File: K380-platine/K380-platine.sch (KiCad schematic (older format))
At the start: 32 parts, among them J1 JST-PH 2, J2 Conn_01x23, J3 MicroMod-M.2E, J4 USB_C_Receptacle_USB2.0, J5 Conn_ARM_JTAG_SWD_10, Q1 PMost Enc FET -20V, Q2 Q_NMOS_DGS, SW1 EG1215AA, SW2 SW_Push, SW3 SW_Push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

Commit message: Finished basic layout
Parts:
- Q2: symbol Device:Q_NMOS_DGS -> Device:Q_NMOS_DSG
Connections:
- net VBAT: now also Q2.2 (S); no longer Q2.3 (S)
- net at R7.1: now also Q2.3 (G); no longer Q2.2 (G)
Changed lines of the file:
@@
 $EndComp
 $Comp
-L Device:Q_NMOS_DGS Q2
+L Device:Q_NMOS_DSG Q2
 U 1 1 62992380
 P 1750 9150

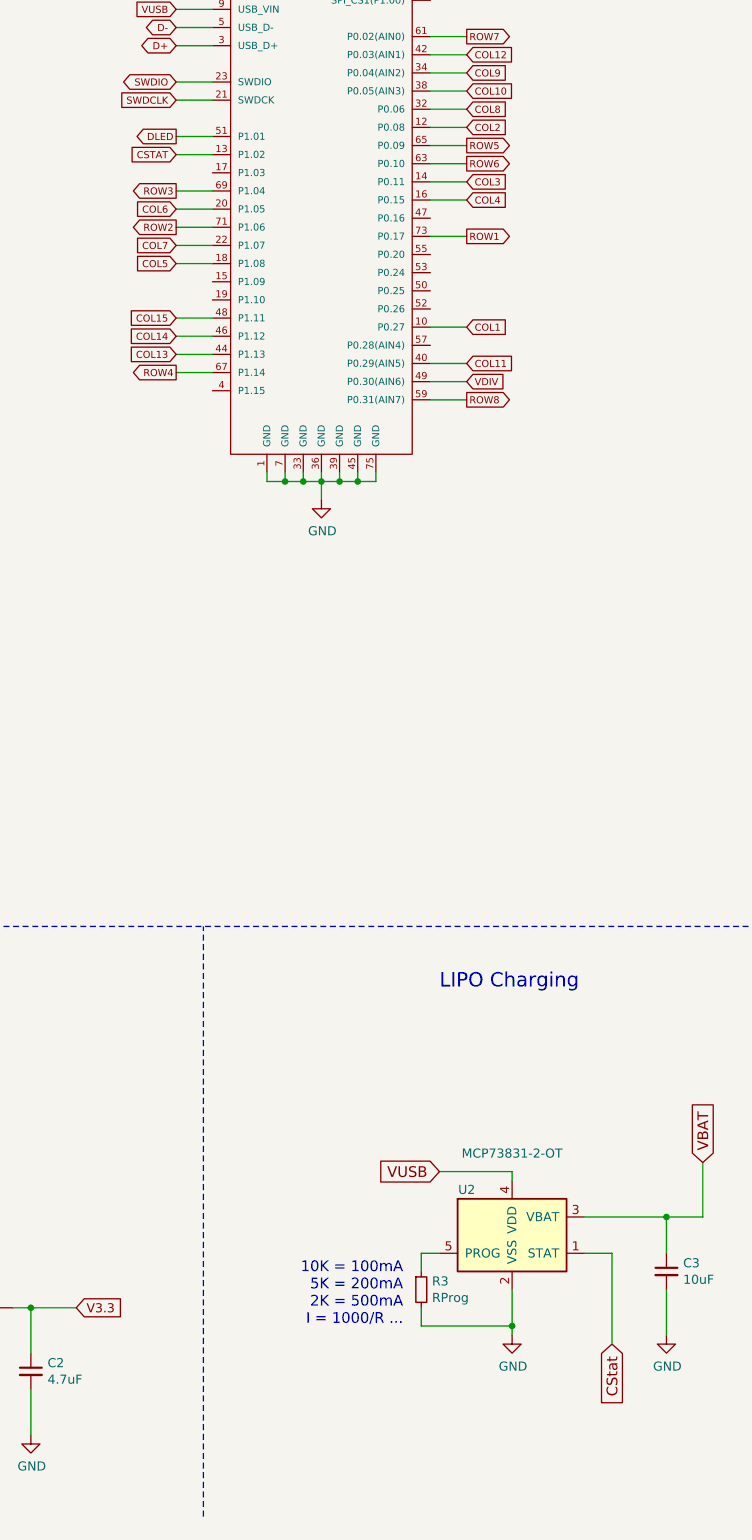
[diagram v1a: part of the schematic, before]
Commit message: Change pin of DLED and CSTAT
- cstat was misspelled so KiCad made no connection
- DLED is closer to where it needs to be
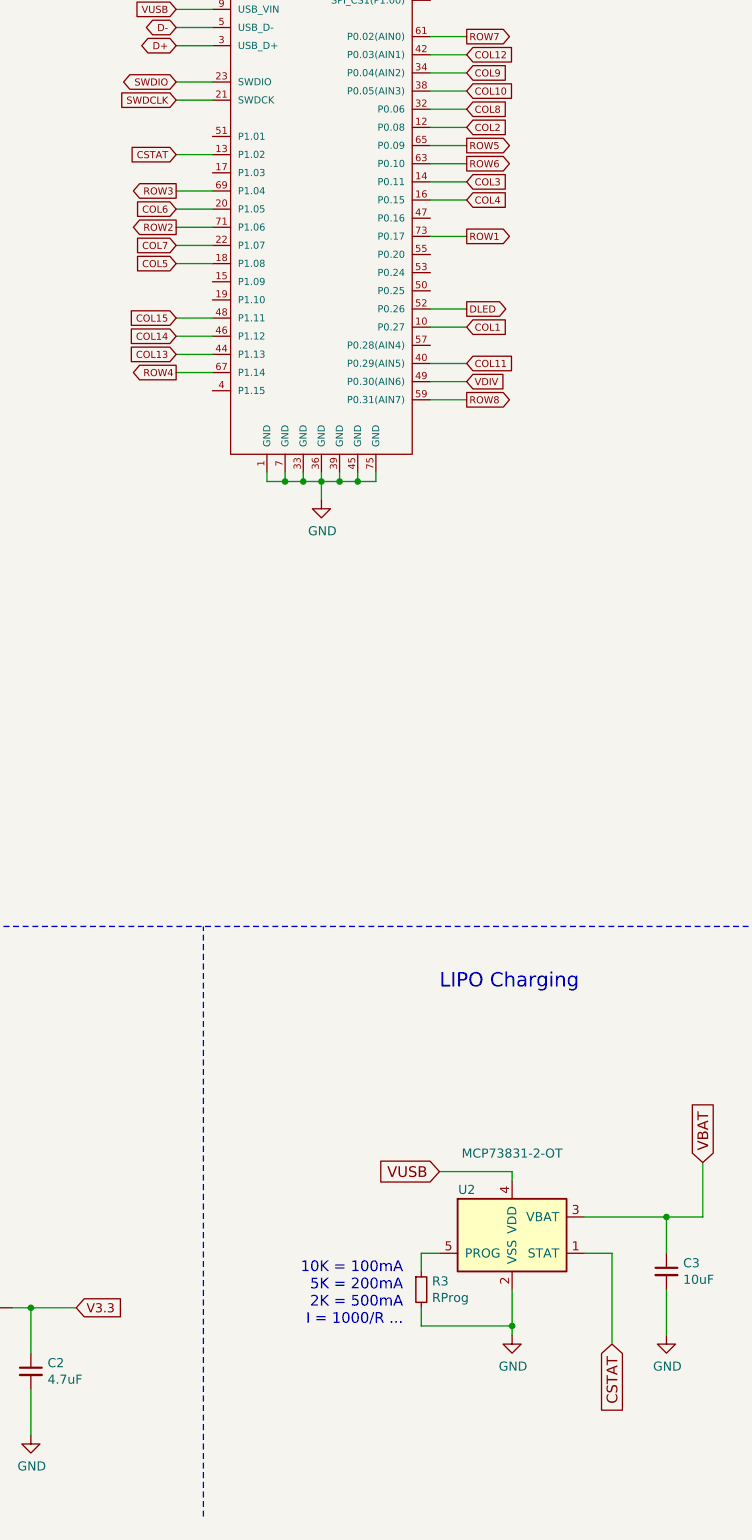
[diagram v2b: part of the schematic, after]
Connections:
- net CStat is gone; now on net CSTAT: U2.1 (STAT)
- net DLED: now also J3.52 (P0.26); no longer J3.51 (P1.01)
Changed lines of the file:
@@
 	6900 10200 6900 9950
 Text GLabel 6600 10250 3    59   Input ~ 0
-CStat
+CSTAT
 Text Notes 5650 8300 0    79   ~ 0
 LIPO Charging
@@
 Text GLabel 5800 4950 2    39   Input ~ 0
 VDIV
-Text GLabel 4200 3600 0    39   Output ~ 0
+Text GLabel 5800 4550 2    39   Output ~ 0
 DLED
 Text GLabel 4200 3700 0    39   Input ~ 0
@@
 	8650 10650 8650 10750
 Wire Wire Line
-	4200 3600 4400 3600
-Wire Wire Line
 	4400 3700 4200 3700
 Wire Wire Line
@@
 Wire Wire Line
 	5600 3050 5800 3050
+Wire Wire Line
+	5800 4550 5600 4550
 $EndSCHEMATC

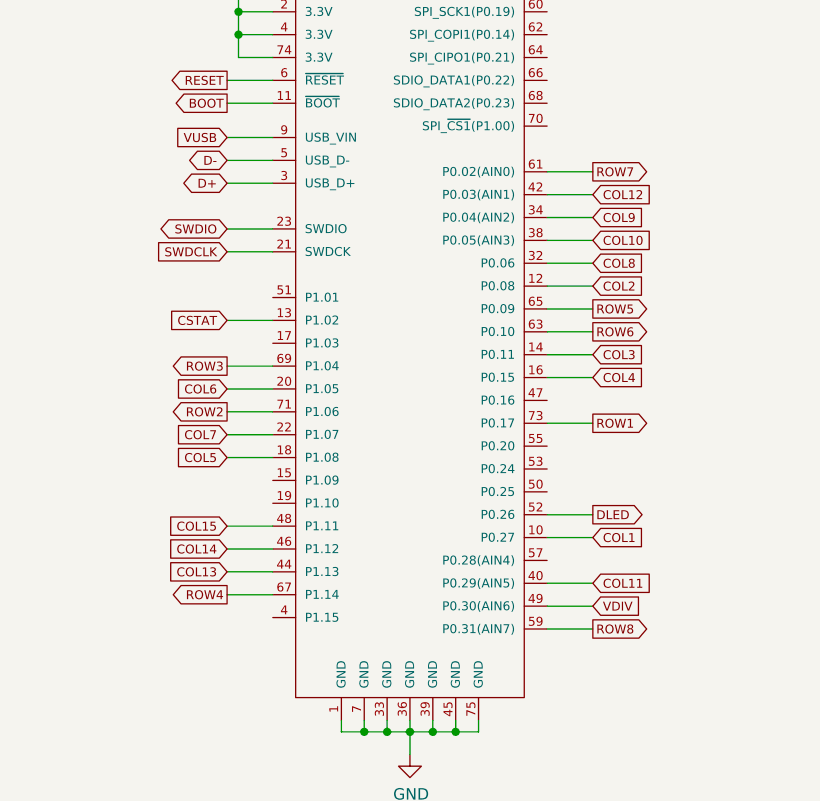
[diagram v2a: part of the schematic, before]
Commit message: Finished routing
- GND is zone fill in bottom
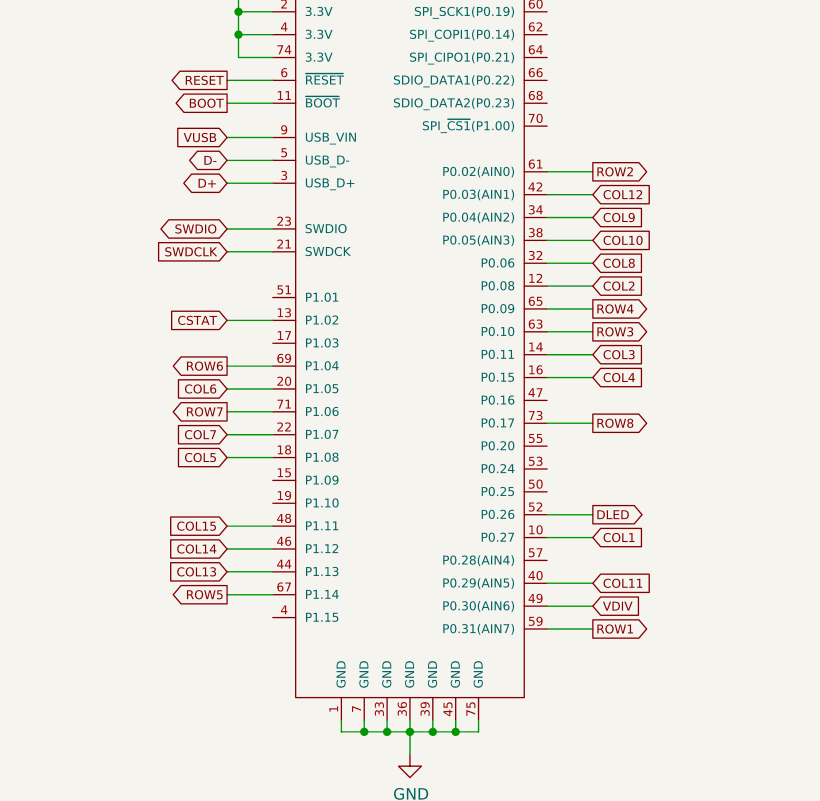
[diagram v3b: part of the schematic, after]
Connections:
- net ROW1: now also J3.59 (P0.31(AIN7)); no longer J3.73 (P0.17)
- net ROW2: now also J3.61 (P0.02(AIN0)); no longer J3.71 (P1.06)
- net ROW3: now also J3.63 (P0.10); no longer J3.69 (P1.04)
- net ROW4: now also J3.65 (P0.09); no longer J3.67 (P1.14)
- net ROW5: now also J3.67 (P1.14); no longer J3.65 (P0.09)
- net ROW6: now also J3.69 (P1.04); no longer J3.63 (P0.10)
- net ROW7: now also J3.71 (P1.06); no longer J3.61 (P0.02(AIN0))
- net ROW8: now also J3.73 (P0.17); no longer J3.59 (P0.31(AIN7))
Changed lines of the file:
@@
 CSTAT
 Text GLabel 5800 4150 2    39   Output ~ 0
+ROW8
+Text GLabel 4200 4900 0    39   Output ~ 0
+ROW5
+Text GLabel 5800 3650 2    39   Output ~ 0
+ROW4
+Text GLabel 5800 3750 2    39   Output ~ 0
+ROW3
+Text GLabel 5800 3050 2    39   Output ~ 0
+ROW2
+Text GLabel 5800 5050 2    39   Output ~ 0
 ROW1
-Text GLabel 4200 4100 0    39   Output ~ 0
-ROW2
-Text GLabel 4200 3900 0    39   Output ~ 0
-ROW3
-Text GLabel 4200 4900 0    39   Output ~ 0
-ROW4
-Text GLabel 5800 3650 2    39   Output ~ 0
-ROW5
-Text GLabel 5800 3750 2    39   Output ~ 0
-ROW6
-Text GLabel 5800 3050 2    39   Output ~ 0
-ROW7
-Text GLabel 5800 5050 2    39   Output ~ 0
-ROW8
 Text GLabel 5800 4650 2    39   Input ~ 0
 COL1
@@
 Wire Wire Line
 	5800 4550 5600 4550
+Text GLabel 4200 4100 0    39   Output ~ 0
+ROW7
+Text GLabel 4200 3900 0    39   Output ~ 0
+ROW6
 $EndSCHEMATC

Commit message: Add test probes
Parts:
- added CSTAT1: T_CSTAT, TestPoint:TestPoint_Pad_D1.0mm, symbol Connector:TestPoint_Probe
- added DLED1: T_DLED, TestPoint:TestPoint_Pad_D1.0mm, symbol Connector:TestPoint_Probe
- added GND1: T_GND, TestPoint:TestPoint_Pad_D1.0mm, symbol Connector:TestPoint_Probe
- added V3.3: T_V3.3, TestPoint:TestPoint_Pad_D1.0mm, symbol Connector:TestPoint_Probe
- added VBAT1: T_VBAT, TestPoint:TestPoint_Pad_D1.0mm, symbol Connector:TestPoint_Probe
- added VUSB1: T_VUSB, TestPoint:TestPoint_Pad_D1.0mm, symbol Connector:TestPoint_Probe
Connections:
- net CSTAT: now also CSTAT1.1
- net DLED: now also DLED1.1
- net GND: now also GND1.1
- net V3.3: now also V3.3.1
- net VBAT: now also VBAT1.1
- net VUSB: now also VUSB1.1
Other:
- note added: "Debug Probes"
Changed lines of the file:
@@
 Wire Notes Line
 	11600 5200 9050 5200
-Wire Notes Line
-	9050 5200 9050 7950
 Text GLabel 4200 3400 0    39   Input ~ 0
 SWDCLK
@@
 Text GLabel 4200 3900 0    39   Output ~ 0
 ROW6
+$Comp
+L Connector:TestPoint_Probe GND1
+U 1 1 62ED9230
+P 10700 4400
+F 0 "GND1" H 10853 4501 50  0000 L CNN
+F 1 "T_GND" H 10853 4410 50  0000 L CNN
+F 2 "TestPoint:TestPoint_Pad_D1.0mm" H 10900 4400 50  0001 C CNN
+F 3 "~" H 10900 4400 50  0001 C CNN
+	1    10700 4400
+	1    0    0    -1
+$EndComp
+$Comp
+L Connector:TestPoint_Probe VUSB1
+U 1 1 62EDA376
+P 10700 4650
+F 0 "VUSB1" H 10853 4751 50  0000 L CNN
+F 1 "T_VUSB" H 10853 4660 50  0000 L CNN
+F 2 "TestPoint:TestPoint_Pad_D1.0mm" H 10900 4650 50  0001 C CNN
+F 3 "~" H 10900 4650 50  0001 C CNN
+	1    10700 4650
+	1    0    0    -1
+$EndComp
+$Comp
+L Connector:TestPoint_Probe V3.3
+U 1 1 62EDAC40
+P 10700 4900
+F 0 "V3.3" H 10852 5001 50  0000 L CNN
+F 1 "T_V3.3" H 10852 4910 50  0000 L CNN
+F 2 "TestPoint:TestPoint_Pad_D1.0mm" H 10900 4900 50  0001 C CNN
+F 3 "~" H 10900 4900 50  0001 C CNN
+	1    10700 4900
+	1    0    0    -1
+$EndComp
+Text GLabel 10700 4900 0    79   Input ~ 0
+V3.3
+Text GLabel 10700 4650 0    79   Input ~ 0
+VUSB
+Text GLabel 10700 4400 0    79   Input ~ 0
+GND
+$Comp
+L Connector:TestPoint_Probe DLED1
+U 1 1 62F54153
+P 9850 4400
+F 0 "DLED1" H 10002 4501 50  0000 L CNN
+F 1 "T_DLED" H 10002 4410 50  0000 L CNN
+F 2 "TestPoint:TestPoint_Pad_D1.0mm" H 10050 4400 50  0001 C CNN
+F 3 "~" H 10050 4400 50  0001 C CNN
+	1    9850 4400
+	1    0    0    -1
+$EndComp
+Text GLabel 9850 4400 0    79   Input ~ 0
+DLED
+$Comp
+L Connector:TestPoint_Probe VBAT1
+U 1 1 62F5DCAD
+P 9850 4650
+F 0 "VBAT1" H 10002 4751 50  0000 L CNN
+F 1 "T_VBAT" H 10002 4660 50  0000 L CNN
+F 2 "TestPoint:TestPoint_Pad_D1.0mm" H 10050 4650 50  0001 C CNN
+F 3 "~" H 10050 4650 50  0001 C CNN
+	1    9850 4650
+	1    0    0    -1
+$EndComp
+Text GLabel 9850 4650 0    79   Input ~ 0
+VBAT
+Text GLabel 9850 4900 0    79   Input ~ 0
+CSTAT
+$Comp
+L Connector:TestPoint_Probe CSTAT1
+U 1 1 62F5F6A8
+P 9850 4900
+F 0 "CSTAT1" H 10003 5001 50  0000 L CNN
+F 1 "T_CSTAT" H 10003 4910 50  0000 L CNN
+F 2 "TestPoint:TestPoint_Pad_D1.0mm" H 10050 4900 50  0001 C CNN
+F 3 "~" H 10050 4900 50  0001 C CNN
+	1    9850 4900
+	1    0    0    -1
+$EndComp
+Text Notes 9850 4000 0    79   ~ 0
+Debug Probes
+Wire Notes Line
+	9050 3700 11600 3700
+Wire Notes Line
+	9050 3700 9050 7950
 $EndSCHEMATC
